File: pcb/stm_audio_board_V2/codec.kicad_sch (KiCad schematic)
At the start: 11 parts, among them Y1 Crystal_GND24

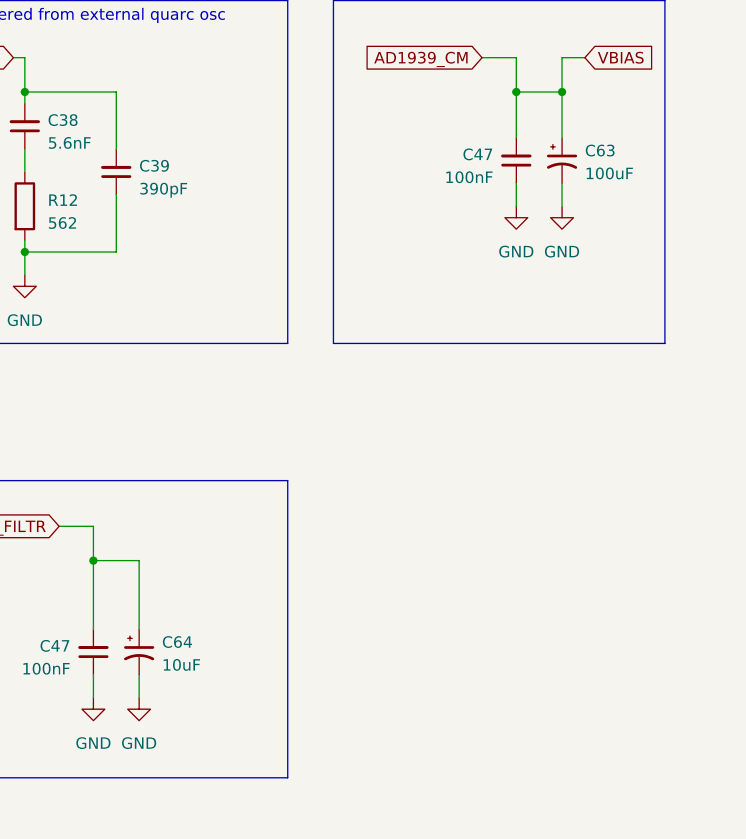
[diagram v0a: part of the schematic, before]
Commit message: Capacitor types are choosen, schematic updated, unused capacitors deleted. Connectors need to be connected to the mcu and its finished
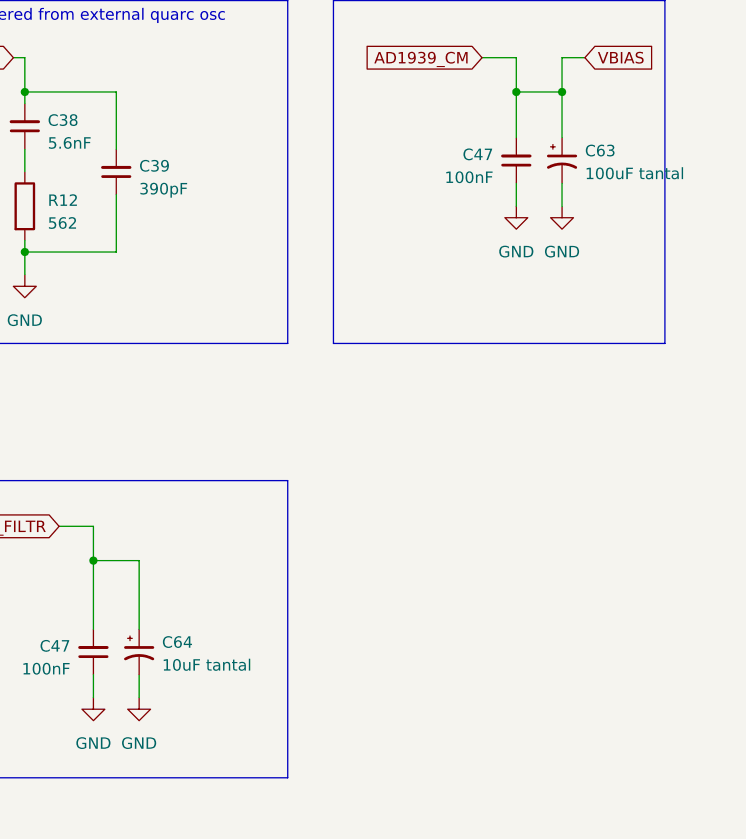
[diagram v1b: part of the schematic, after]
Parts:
- C38: footprint Capacitor_SMD:C_0603_1608Metric_Pad1.08x0.95mm_HandSolder -> Capacitor_SMD:C_0805_2012Metric_Pad1.18x1.45mm_HandSolder
- C63: value 100uF -> 100uF tantal; footprint Capacitor_SMD:CP_Elec_6.3x7.7 -> Capacitor_Tantalum_SMD:CP_EIA-7343-31_Kemet-D_Pad2.25x2.55mm_HandSolder
- C64: value 10uF -> 10uF tantal; footprint Capacitor_SMD:C_1210_3225Metric_Pad1.33x2.70mm_HandSolder -> Capacitor_SMD:C_0805_2012Metric_Pad1.18x1.45mm_HandSolder
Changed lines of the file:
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@@
       (effects (font (size 1.27 1.27)) (justify left))
     )
-    (property "Value" "10uF" (at 167.64 104.3432 0)
+    (property "Value" "10uF tantal" (at 167.64 104.3432 0)
       (effects (font (size 1.27 1.27)) (justify left))
     )
-    (property "Footprint" "Capacitor_SMD:C_1210_3225Metric_Pad1.33x2.70mm_HandSolder" (at 165.1 102.87 0)
+    (property "Footprint" "Capacitor_SMD:C_0805_2012Metric_Pad1.18x1.45mm_HandSolder" (at 165.1 102.87 0)
       (effects (font (size 1.27 1.27)) hide)
     )
@@
       (effects (font (size 1.27 1.27)) (justify right))
     )
-    (property "Footprint" "Capacitor_SMD:C_0603_1608Metric_Pad1.08x0.95mm_HandSolder" (at 152.4 44.45 0)
+    (property "Footprint" "Capacitor_SMD:C_0805_2012Metric_Pad1.18x1.45mm_HandSolder" (at 152.4 44.45 0)
       (effects (font (size 1.27 1.27)) hide)
     )
@@
       (effects (font (size 1.27 1.27)) (justify left))
     )
-    (property "Value" "100uF" (at 214.63 49.7332 0)
+    (property "Value" "100uF tantal" (at 214.63 49.7332 0)
       (effects (font (size 1.27 1.27)) (justify left))
     )
-    (property "Footprint" "Capacitor_SMD:CP_Elec_6.3x7.7" (at 212.09 48.26 0)
-      (effects (font (size 1.27 1.27)) hide)
-    )
-    (property "Datasheet" "~" (at 212.09 48.26 0)
-      (effects (font (size 1.27 1.27)) hide)
-    )
+    (property "Footprint" "Capacitor_Tantalum_SMD:CP_EIA-7343-31_Kemet-D_Pad2.25x2.55mm_HandSolder" (at 212.09 48.26 0)
+      (effects (font (size 1.27 1.27)) hide)
+    )
+    (property "Datasheet" "https://www.hestore.hu/prod_10032010.html" (at 212.09 48.26 0)
+      (effects (font (size 1.27 1.27)) hide)
+    )

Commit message: pcb seems to be finished drc error: 0
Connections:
- net AD1939_I2S2_SDO: now also U11.19 (DSDATA2); no longer U11.20 (DSDATA1)
- net DAC1L: now also U11.41 (OL2N); no longer U11.37 (OL1N)
- net DAC1R: now also U11.40 (OL2P); no longer U11.36 (OL1P)
- net DAC2L: now also U11.43 (OR2N); no longer U11.39 (OR1N)
- net DAC2R: now also U11.42 (OR2P); no longer U11.38 (OR1P)
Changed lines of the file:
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@@
   (no_connect (at 92.71 118.11))
   (no_connect (at 44.45 63.5))
-  (no_connect (at 92.71 57.15))
+  (no_connect (at 92.71 46.99))
   (no_connect (at 92.71 64.77))
+  (no_connect (at 92.71 41.91))
+  (no_connect (at 92.71 44.45))
   (no_connect (at 44.45 55.88))
   (no_connect (at 92.71 67.31))
-  (no_connect (at 92.71 120.65))
+  (no_connect (at 92.71 123.19))
   (no_connect (at 44.45 45.72))
-  (no_connect (at 92.71 52.07))
+  (no_connect (at 92.71 39.37))
   (no_connect (at 92.71 72.39))
   (no_connect (at 92.71 69.85))
   (no_connect (at 92.71 80.01))
-  (no_connect (at 92.71 54.61))
   (no_connect (at 44.45 118.11))
   (no_connect (at 44.45 58.42))
-  (no_connect (at 92.71 59.69))
   (no_connect (at 44.45 48.26))
   (no_connect (at 92.71 85.09))
@@
     (stroke (width 0) (type default))
   )
+  (wire (pts (xy 92.71 120.65) (xy 97.79 120.65))
+    (stroke (width 0) (type default))
+  )
   (wire (pts (xy 152.4 58.42) (xy 152.4 60.96))
     (stroke (width 0) (type default))
@@
     (stroke (width 0) (type default))
   )
-  (wire (pts (xy 96.52 39.37) (xy 92.71 39.37))
+  (wire (pts (xy 97.79 52.07) (xy 92.71 52.07))
     (stroke (width 0) (type default))
   )
@@
     (stroke (width 0) (type default))
   )
-  (wire (pts (xy 92.71 123.19) (xy 97.79 123.19))
-    (stroke (width 0) (type default))
-  )
   (wire (pts (xy 30.48 163.83) (xy 30.48 176.53))
     (stroke (width 0) (type default))
@@
     (stroke (width 0) (type default))
   )
-  (wire (pts (xy 96.52 46.99) (xy 92.71 46.99))
-    (stroke (width 0) (type default))
-  )
   (wire (pts (xy 34.29 109.22) (xy 44.45 109.22))
     (stroke (width 0) (type default))
@@
     (stroke (width 0) (type default))
   )
+  (wire (pts (xy 97.79 57.15) (xy 92.71 57.15))
+    (stroke (width 0) (type default))
+  )
   (wire (pts (xy 92.71 111.76) (xy 97.79 111.76))
     (stroke (width 0) (type default))
@@
     (stroke (width 0) (type default))
   )
+  (wire (pts (xy 97.79 54.61) (xy 92.71 54.61))
+    (stroke (width 0) (type default))
+  )
   (wire (pts (xy 41.91 76.2) (xy 44.45 76.2))
     (stroke (width 0) (type default))
@@
     (stroke (width 0) (type default))
   )
-  (wire (pts (xy 96.52 44.45) (xy 92.71 44.45))
-    (stroke (width 0) (type default))
-  )
   (wire (pts (xy 26.67 156.21) (xy 26.67 170.18))
     (stroke (width 0) (type default))
@@
     (stroke (width 0) (type default))
   )
+  (wire (pts (xy 97.79 59.69) (xy 92.71 59.69))
+    (stroke (width 0) (type default))
+  )
   (wire (pts (xy 30.48 176.53) (xy 36.83 176.53))
     (stroke (width 0) (type default))
@@
     (stroke (width 0) (type default))
   )
-  (wire (pts (xy 96.52 41.91) (xy 92.71 41.91))
-    (stroke (width 0) (type default))
-  )
   (wire (pts (xy 40.64 170.18) (xy 46.99 170.18))
     (stroke (width 0) (type default))
@@
     )
   )
-  (global_label "AD1939_I2S2_SDO" (shape input) (at 97.79 123.19 0) (fields_autoplaced)
-    (effects (font (size 1.27 1.27)) (justify left))
-    (property "Intersheetrefs" "${INTERSHEET_REFS}" (at 117.8709 123.19 0)
+  (global_label "AD1939_I2S2_SDO" (shape input) (at 97.79 120.65 0) (fields_autoplaced)
+    (effects (font (size 1.27 1.27)) (justify left))
+    (property "Intersheetrefs" "${INTERSHEET_REFS}" (at 117.8709 120.65 0)
       (effects (font (size 1.27 1.27)) (justify left) hide)
     )
@@
     )
   )
-  (global_label "DAC1L" (shape input) (at 96.52 44.45 0) (fields_autoplaced)
-    (effects (font (size 1.27 1.27)) (justify left))
-    (property "Intersheetrefs" "${INTERSHEET_REFS}" (at 105.292 44.45 0)
+  (global_label "DAC1L" (shape input) (at 97.79 57.15 0) (fields_autoplaced)
+    (effects (font (size 1.27 1.27)) (justify left))
+    (property "Intersheetrefs" "${INTERSHEET_REFS}" (at 106.562 57.15 0)
       (effects (font (size 1.27 1.27)) (justify left) hide)
     )
@@
     )
   )
-  (global_label "DAC2L" (shape input) (at 96.52 39.37 0) (fields_autoplaced)
-    (effects (font (size 1.27 1.27)) (justify left))
-    (property "Intersheetrefs" "${INTERSHEET_REFS}" (at 105.292 39.37 0)
+  (global_label "DAC2L" (shape input) (at 97.79 52.07 0) (fields_autoplaced)
+    (effects (font (size 1.27 1.27)) (justify left))
+    (property "Intersheetrefs" "${INTERSHEET_REFS}" (at 106.562 52.07 0)
       (effects (font (size 1.27 1.27)) (justify left) hide)
     )
@@
     )
   )
-  (global_label "DAC2R" (shape input) (at 96.52 41.91 0) (fields_autoplaced)
-    (effects (font (size 1.27 1.27)) (justify left))
-    (property "Intersheetrefs" "${INTERSHEET_REFS}" (at 105.5339 41.91 0)
+  (global_label "DAC2R" (shape input) (at 97.79 54.61 0) (fields_autoplaced)
+    (effects (font (size 1.27 1.27)) (justify left))
+    (property "Intersheetrefs" "${INTERSHEET_REFS}" (at 106.8039 54.61 0)
       (effects (font (size 1.27 1.27)) (justify left) hide)
     )
@@
     )
   )
-  (global_label "DAC1R" (shape input) (at 96.52 46.99 0) (fields_autoplaced)
-    (effects (font (size 1.27 1.27)) (justify left))
-    (property "Intersheetrefs" "${INTERSHEET_REFS}" (at 105.5339 46.99 0)
-      (effects (font (size 1.27 1.27)) (justify left) hide)
-    )
+  (global_label "DAC1R" (shape input) (at 97.79 59.69 0) (fields_autoplaced)
+    (effects (font (size 1.27 1.27)) (justify left))
+    (property "Intersheetrefs" "${INTERSHEET_REFS}" (at 106.8039 59.69 0)
+      (effects (font (size 1.27 1.27)) (justify left) hide)
+    )

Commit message: added vias and overall fixes around pcb
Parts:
- C64: footprint Capacitor_SMD:C_0805_2012Metric_Pad1.18x1.45mm_HandSolder -> Capacitor_Tantalum_SMD:CP_EIA-6032-28_Kemet-C_Pad2.25x2.35mm_HandSolder
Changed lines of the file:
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@@
       (effects (font (size 1.27 1.27)) (justify left))
     )
-    (property "Footprint" "Capacitor_SMD:C_0805_2012Metric_Pad1.18x1.45mm_HandSolder" (at 165.1 102.87 0)
+    (property "Footprint" "Capacitor_Tantalum_SMD:CP_EIA-6032-28_Kemet-C_Pad2.25x2.35mm_HandSolder" (at 165.1 102.87 0)
       (effects (font (size 1.27 1.27)) hide)
     )

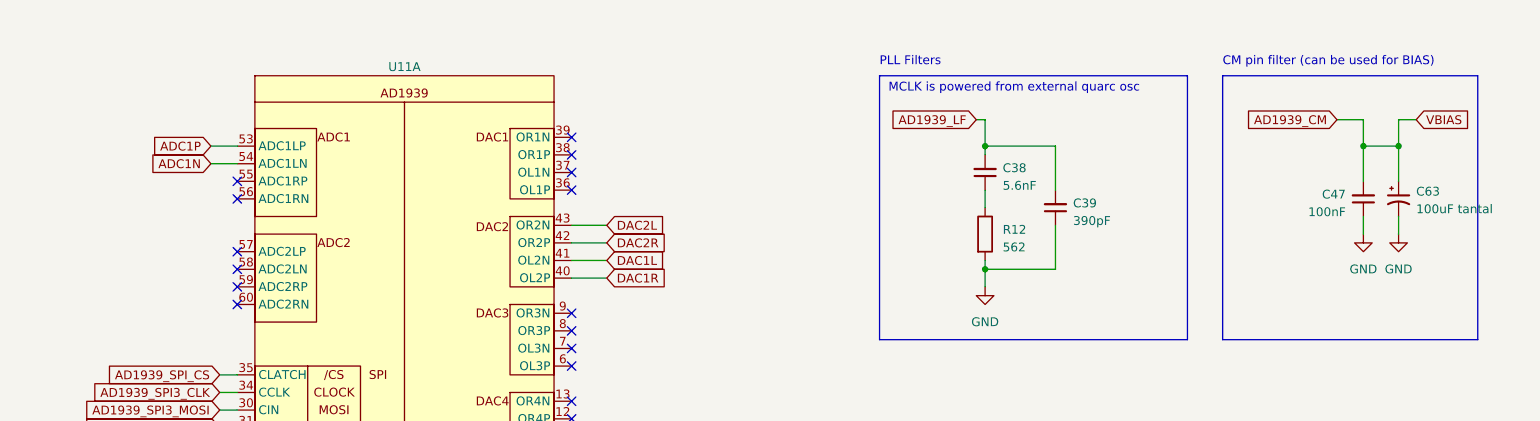
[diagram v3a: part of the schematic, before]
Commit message: stm_audio_board_V2 is finished, sent to jlcPCB for production
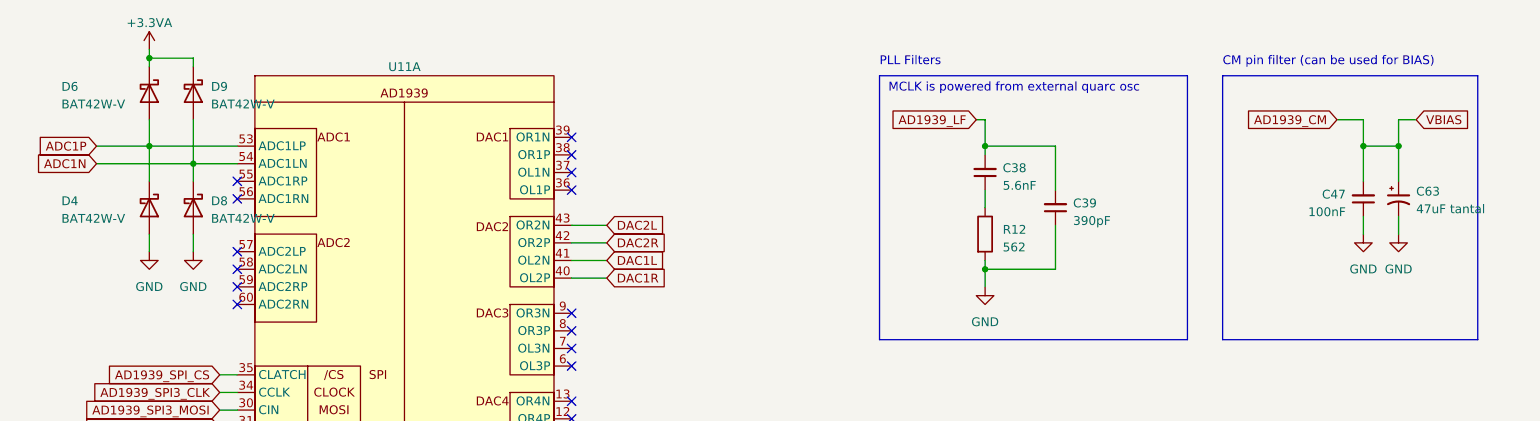
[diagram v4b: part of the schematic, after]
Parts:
- added D4, D6, D8, D9: BAT42W-V, Diode_SMD:D_SOD-123, symbol Diode:BAT42W-V
- C63: value 100uF tantal -> 47uF tantal
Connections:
- net ADC1N: now also D8.1 (K), D9.2 (A)
- net ADC1P: now also D4.1 (K), D6.2 (A)
- net GND: now also D4.2 (A), D8.2 (A)
- new net +3.3VA: D6.1 (K), D9.1 (K)
